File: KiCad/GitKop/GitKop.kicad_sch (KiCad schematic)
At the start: 39 parts, among them J1 POWER_Socket, J2 Conn_01x08_Socket, J3 Conn_01x04_Socket, J4 RJ45, Q1 BC557, Q2 BC547, Q3 IRF740, SW1 RotaryEncoder_Switch, U1 MCP6281, U2 TL071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

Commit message: kicad: updated
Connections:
- net COIL1: now also RV1.2; no longer RV1.3
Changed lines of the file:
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@@
-	)
-	(junction
-		(at 130.81 128.27)
-		(diameter 0)
-		(color 0 0 0 0)
 	)
 	(junction
@@
 	)
 	(junction
+		(at 127 128.27)
+		(diameter 0)
+		(color 0 0 0 0)
+	)
+	(junction
 		(at 40.64 113.03)
 		(diameter 0)
@@
 	(wire
 		(pts
-			(xy 120.65 128.27) (xy 130.81 128.27)
+			(xy 120.65 128.27) (xy 127 128.27)
 		)
 		(stroke
@@
 	(wire
 		(pts
+			(xy 127 128.27) (xy 132.08 128.27)
+		)
+		(stroke
+			(width 0)
+			(type default)
+		)
+	)
+	(wire
+		(pts
 			(xy 238.76 48.26) (xy 243.84 48.26)
 		)
@@
 	(wire
 		(pts
-			(xy 130.81 128.27) (xy 132.08 128.27)
-		)
-		(stroke
-			(width 0)
-			(type default)
-		)
-	)
-	(wire
-		(pts
 			(xy 50.8 64.77) (xy 43.18 64.77)
 		)
@@
 	(wire
 		(pts
-			(xy 130.81 128.27) (xy 130.81 138.43)
-		)
-		(stroke
-			(width 0)
-			(type default)
-		)
-	)
-	(wire
-		(pts
 			(xy 142.24 128.27) (xy 142.24 138.43)
 		)
@@
 		)
 		(stroke
+			(width 0)
+			(type default)
+		)
+	)
+	(wire
+		(pts
+			(xy 127 128.27) (xy 127 142.24)
+		)
+		(stroke

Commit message: sch: r5, r6 real values
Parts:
- R5: value 2000 -> 130
- R6: value 1000 -> 3100
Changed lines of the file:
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@@
 			)
 		)
-		(property "Value" "1000"
+		(property "Value" "3100"
 			(at 135.89 124.46 90)
 			(effects
@@
 		(fields_autoplaced yes)
 		(property "Reference" "R5"
-			(at 118.11 140.9699 0)
-			(effects
-				(font
-					(size 1.27 1.27)
-				)
-				(justify right)
-			)
-		)
-		(property "Value" "2000"
-			(at 118.11 143.5099 0)
-			(effects
-				(font
-					(size 1.27 1.27)
-				)
-				(justify right)
-			)
-		)
+			(at 123.19 140.9699 0)
+			(effects
+				(font
+					(size 1.27 1.27)
+				)
+				(justify left)
+			)
+		)
+		(property "Value" "130"
+			(at 123.19 143.5099 0)
+			(effects
+				(font
+					(size 1.27 1.27)
+				)
+				(justify left)
+			)
+		)

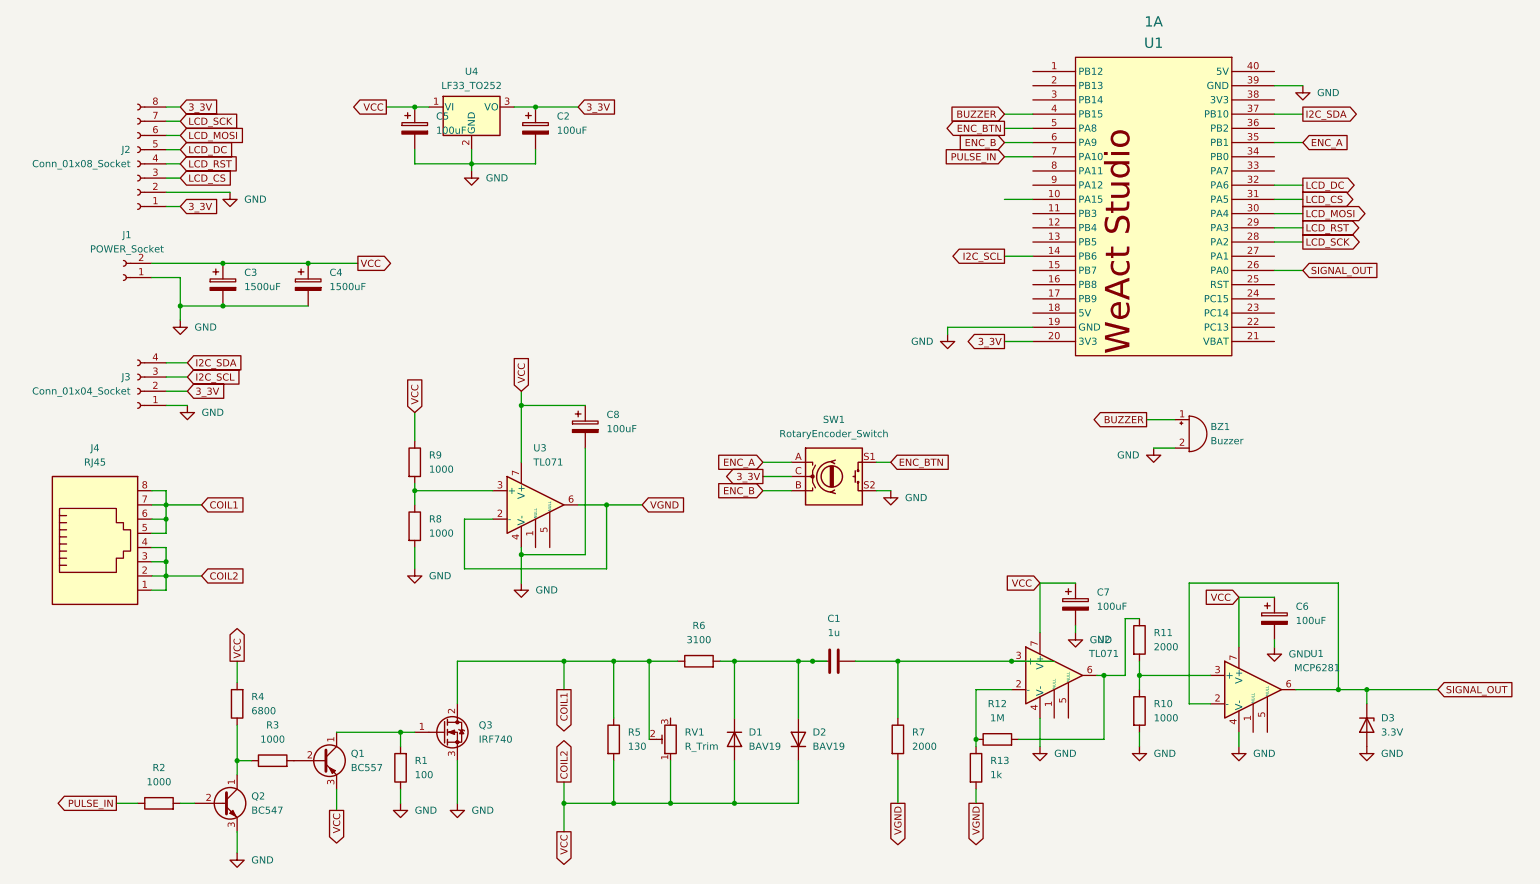
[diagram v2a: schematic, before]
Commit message: sch: cleanup and textbox
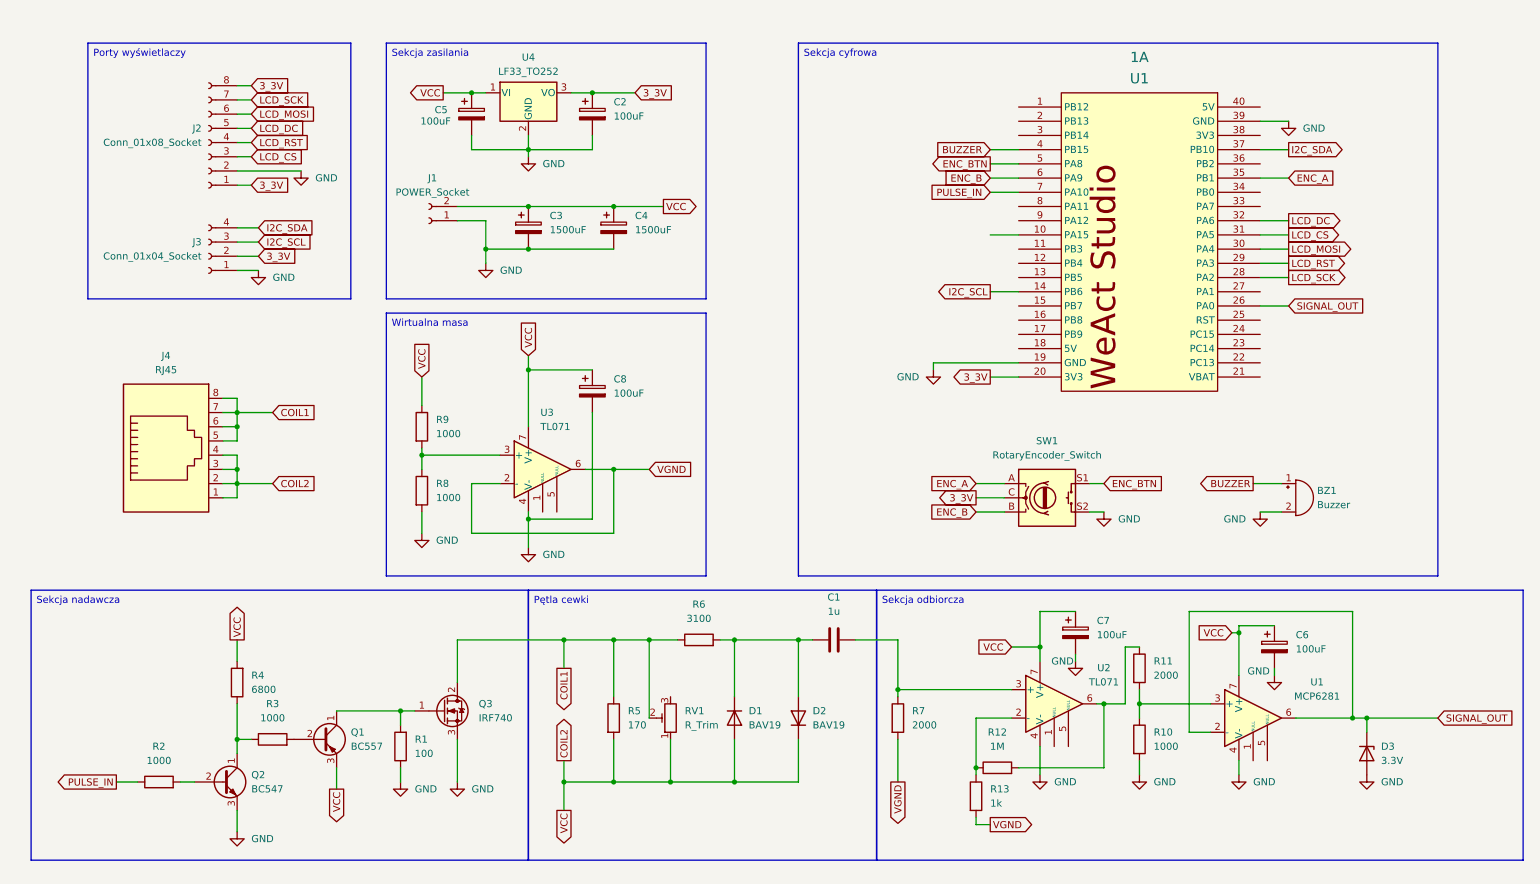
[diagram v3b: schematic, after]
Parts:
- R5: value 130 -> 170
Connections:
- net at C1.2, R7.1, U2.3 (+): no longer U2.8 (NC)
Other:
- company: Gitcorp -> Pawel Reich
- moved on the sheet: 1A, BZ1, C1, C2, C3, C4, C5, C6, C7, C8, D1, D2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

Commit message: sch: fix mcp6281 vcc
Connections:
- net 3_3V: now also C6.1, U1.7 (V+)
- net COIL2: no longer C6.1, U1.7 (V+)
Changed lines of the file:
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@@
 		)
 	)
-	(global_label "VCC"
+	(global_label "3_3V"
 		(shape input)
 		(at 231.14 123.19 180)
@@
 		)
 		(property "Intersheetrefs" "${INTERSHEET_REFS}"
-			(at 224.5262 123.19 0)
+			(at 223.6796 123.19 0)
 			(effects
 				(font
